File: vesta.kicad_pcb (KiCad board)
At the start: 4 copper layers, 43 x 61.1 mm, 59 parts, among them J1 Solar Panel, J2 Solar Panel, J3 Conn_ARM_SWD_TagConnect_TC203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, J4 U.FL, U1 STM32WL55CCU6, U2 BQ24074RGTR, U3 TPS63900DSKR, U4 BME688_C3664478, U6 PE4259-63, X1 Q13FC1350000400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

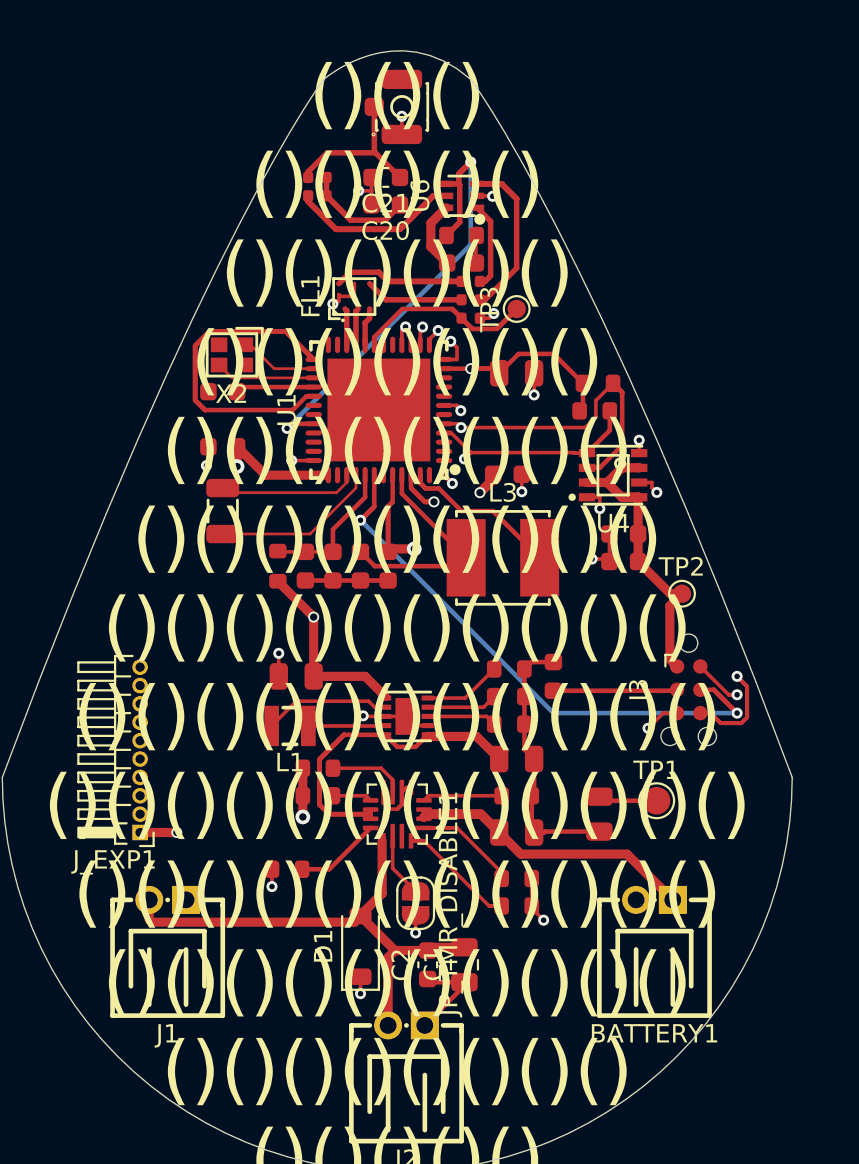
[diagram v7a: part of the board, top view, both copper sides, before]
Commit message: feat: stabilize critical connections
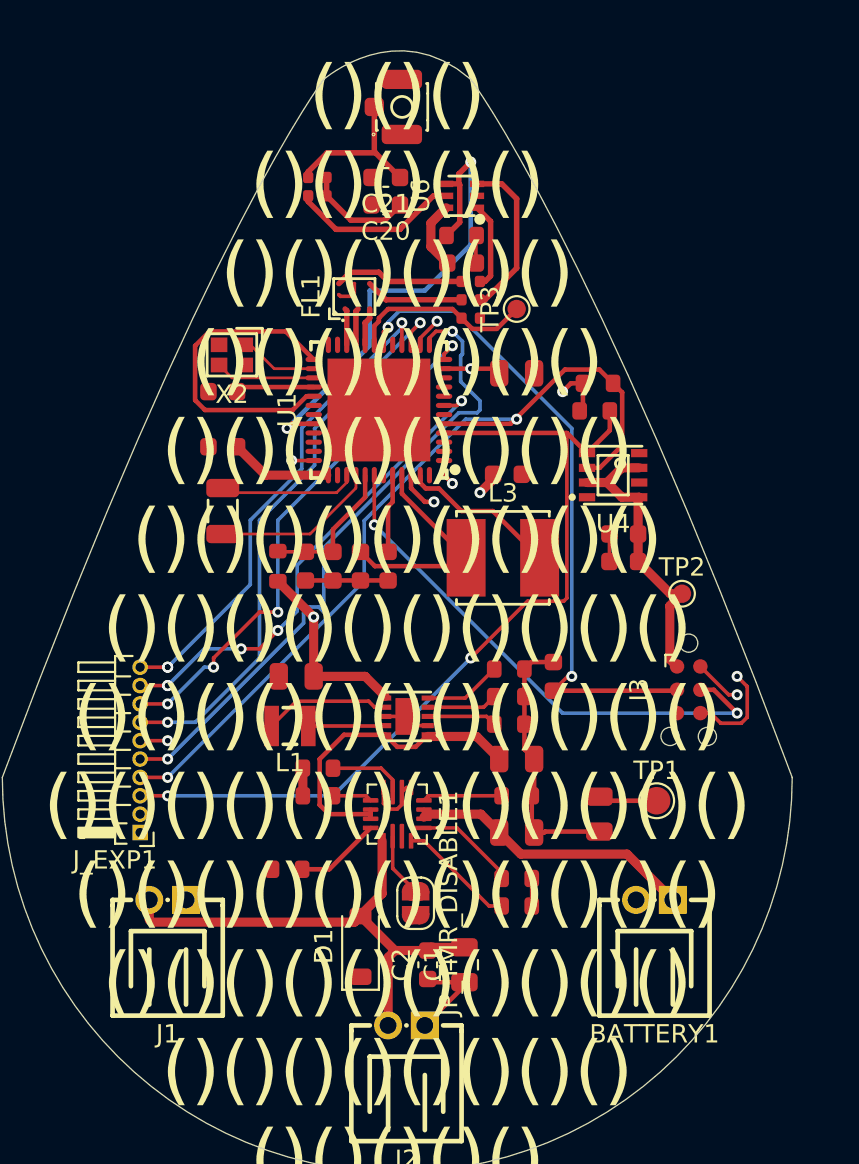
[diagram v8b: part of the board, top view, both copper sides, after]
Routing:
- net /SWDIO: track 38.0 -> 3.84 mm
- net /SPI1_MOSI: track 0.00 -> 31.2 mm, vias 0 -> 2
- net /NRST: track 6.75 -> 35.8 mm, vias 0 -> 2
- net /SPI1_MISO: track 29.9 -> 3.17 mm, vias 1 -> 2
- net GND: track 60.3 -> 36.9 mm, vias 19 -> 0
- net /SMPS_1V55: track 49.3 -> 30.0 mm
- net /3V3_SYS: track 73.8 -> 55.5 mm, vias 8 -> 5
- net Net-(U6-RFC): track 22.8 -> 9.20 mm
- net /I2C1_SCL: track 37.7 -> 47.7 mm, vias 1 -> 2
- net /SWO: track 16.3 -> 6.80 mm
- net /SYS_RAW: track 29.9 -> 20.6 mm
- net /SPI1_SCK: track 31.0 -> 35.7 mm, vias 1 -> 2
- net /RFO_OUT: track 11.9 -> 7.19 mm
- net /BAT_RAW: track 20.5 -> 16.1 mm
- net /SWCLK: track 33.0 -> 29.2 mm
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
